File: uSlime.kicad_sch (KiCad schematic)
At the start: 0 parts

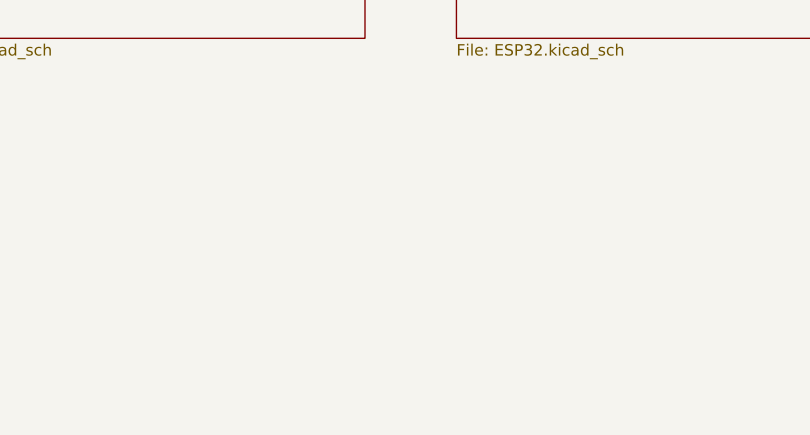
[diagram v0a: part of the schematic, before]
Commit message: Insert ESP32-C6FH4
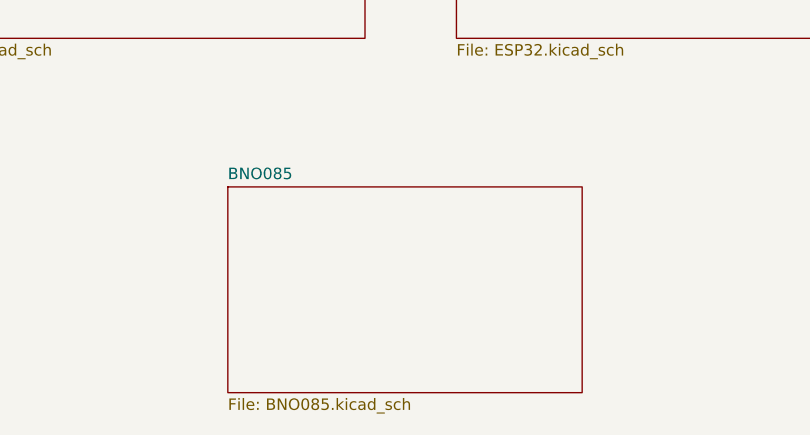
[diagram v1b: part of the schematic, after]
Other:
- added sheet BNO085 (BNO085.kicad_sch)
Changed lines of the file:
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@@
 	(paper "A4")
+	(sheet
+		(at 104.14 81.28)
+		(size 39.37 22.86)
+		(fields_autoplaced yes)
+		(stroke
+			(width 0.1524)
+			(type solid)
+		)
+		(fill
+			(color 0 0 0 0.0000)
+		)
+		(property "Sheetname" "BNO085"
+			(at 104.14 80.5684 0)
+			(effects
+				(font
+					(size 1.27 1.27)
+				)
+				(justify left bottom)
+			)
+		)
+		(property "Sheetfile" "BNO085.kicad_sch"
+			(at 104.14 104.7246 0)
+			(effects
+				(font
+					(size 1.27 1.27)
+				)
+				(justify left top)
+			)
+		)
+		(instances
+			(project "uSlime"
+				(path "/f32c1c49-f803-4e7c-a530-6db148a7ba36"
+					(page "4")
+				)
+			)
+		)
+	)
 	(sheet
 		(at 129.54 21.59)
